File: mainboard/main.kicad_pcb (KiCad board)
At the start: 2 copper layers, 82.5 x 63.5 mm, 36 parts

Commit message: Updated component values in layout
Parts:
- Con_AddOn1: value Conn_01x05 -> Conn_01x09
- Con_P_Sw1: value Conn_01x04 -> Conn_01x02
- Con_RPi1: value Conn_01x05 -> Conn_01x08
- Con_Switch1: value Conn_01x04 -> Conn_01x03
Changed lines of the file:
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@@
       (effects (font (size 1 1) (thickness 0.15)))
     )
-    (fp_text value Conn_01x04 (at 2.54 -3.81 90) (layer F.Fab)
+    (fp_text value Conn_01x03 (at 2.54 -3.81 90) (layer F.Fab)
       (effects (font (size 1 1) (thickness 0.15)))
     )
@@
       (effects (font (size 1 1) (thickness 0.15)))
     )
-    (fp_text value Conn_01x05 (at 2.54 2.54 90) (layer F.Fab)
+    (fp_text value Conn_01x08 (at 2.54 2.54 90) (layer F.Fab)
       (effects (font (size 1 1) (thickness 0.15)))
     )
@@
       (effects (font (size 1 1) (thickness 0.15)))
     )
-    (fp_text value Conn_01x05 (at 17.145 2.54 90) (layer F.Fab)
+    (fp_text value Conn_01x09 (at 17.145 2.54 90) (layer F.Fab)
       (effects (font (size 1 1) (thickness 0.15)))
     )
@@
       (effects (font (size 1 1) (thickness 0.15)))
     )
-    (fp_text value Conn_01x04 (at 10.16 1.27) (layer F.Fab)
-      (effects (font (size 1 1) (thickness 0.15)))
-    )
+    (fp_text value Conn_01x02 (at 10.16 1.27) (layer F.Fab)
+      (effects (font (size 1 1) (thickness 0.15)))
+    )

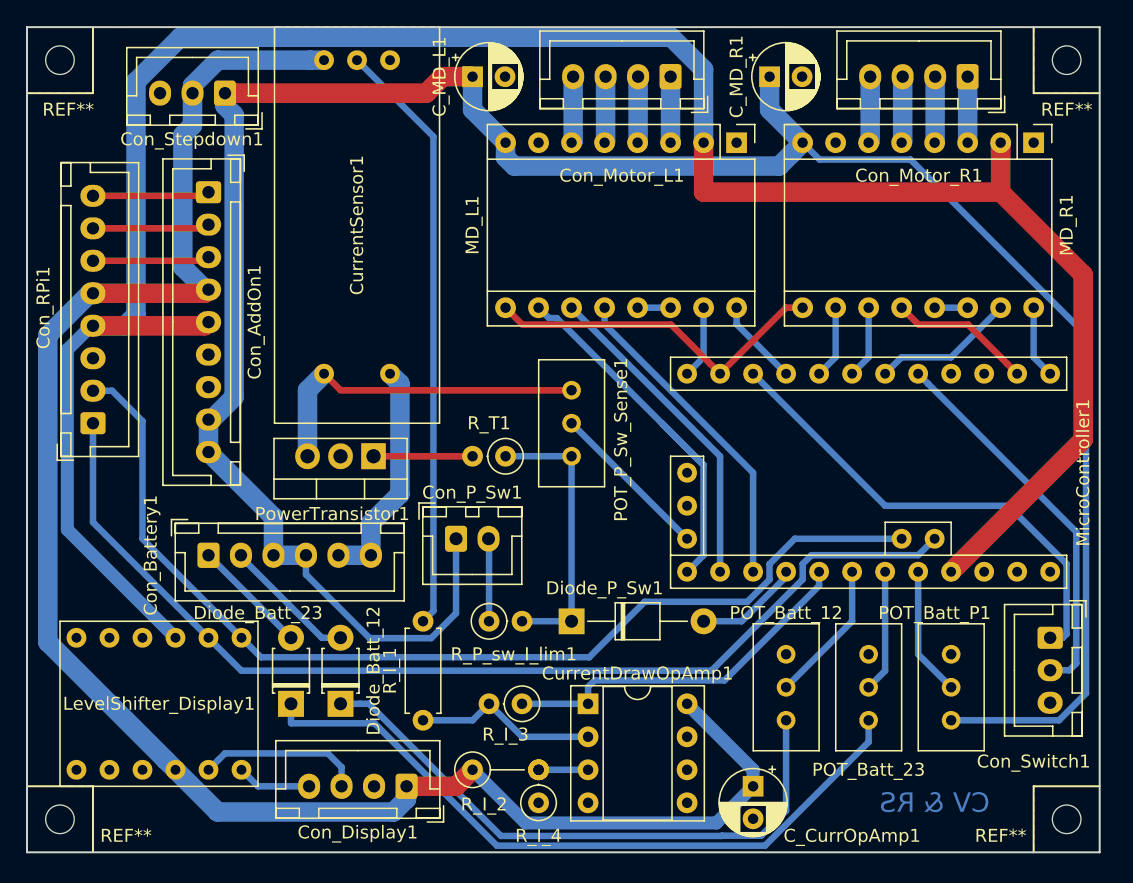
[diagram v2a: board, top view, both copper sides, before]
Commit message: New power circuitry and layout
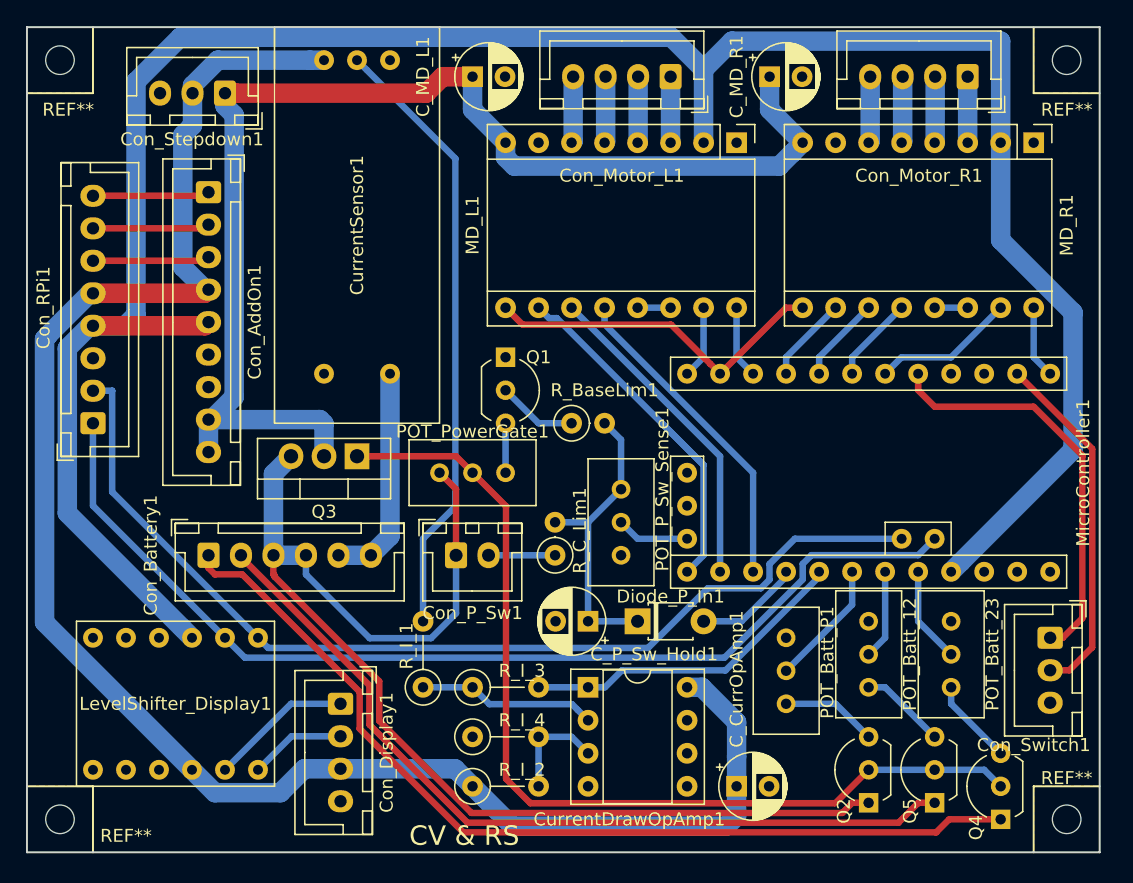
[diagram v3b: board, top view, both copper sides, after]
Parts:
- removed Diode_Batt_12, Diode_Batt_23: 1N 4448, Diode_THT:D_T-1_P5.08mm_Horizontal
- removed Diode_P_Sw1: 1N 4448, Diode_THT:D_T-1_P10.16mm_Horizontal
- removed PowerTransistor1: TIP120, Package_TO_SOT_THT:TO-220-3_Vertical
- removed R_P_sw_I_lim1: optional, Resistor_THT:R_Axial_DIN0207_L6.3mm_D2.5mm_P2.54mm_Vertical
- removed R_T1: 1K, Resistor_THT:R_Axial_DIN0207_L6.3mm_D2.5mm_P2.54mm_Vertical
- added C_P_Sw_Hold1: 100uF, Capacitor_THT:CP_Radial_D5.0mm_P2.50mm, F.Cu at (153.7, 72.4)
- added Diode_P_In1: 1N 4448, Diode_THT:D_T-1_P5.08mm_Horizontal, F.Cu at (157.5, 72.4)
- added POT_PowerGate1: 100K, Potentiometer_THT:Potentiometer_Bourns_3296W_Vertical, F.Cu at (142.2, 61.0)
- added Q1: 2N3904, Package_TO_SOT_THT:TO-92_Inline_Wide, F.Cu at (147.3, 52.1)
- added Q2: ZVP2106A, Package_TO_SOT_THT:TO-92L_Inline_Wide, F.Cu at (175.3, 86.4)
- added Q3: STP10P6F6, Package_TO_SOT_THT:TO-220-3_Vertical, F.Cu at (135.9, 59.7)
- added Q4: ZVP2106A, Package_TO_SOT_THT:TO-92L_Inline_Wide, F.Cu at (185.4, 87.6)
- added Q5: ZVP2106A, Package_TO_SOT_THT:TO-92L_Inline_Wide, F.Cu at (180.3, 86.4)
- added R_BaseLim1: 10k, Resistor_THT:R_Axial_DIN0207_L6.3mm_D2.5mm_P2.54mm_Vertical, F.Cu at (152.4, 57.1)
- added R_C_Lim1: 220, Resistor_THT:R_Axial_DIN0207_L6.3mm_D2.5mm_P2.54mm_Vertical, F.Cu at (151.1, 67.3)
- POT_Batt_12, POT_Batt_23, POT_Batt_P1: value 1M -> 100k
- POT_P_Sw_Sense1: value 50k -> 100K
- R_I_1: footprint Resistor_THT:R_Axial_DIN0207_L6.3mm_D2.5mm_P7.62mm_Horizontal -> Resistor_THT:R_Axial_DIN0207_L6.3mm_D2.5mm_P5.08mm_Vertical
- R_I_3, R_I_4: footprint Resistor_THT:R_Axial_DIN0207_L6.3mm_D2.5mm_P2.54mm_Vertical -> Resistor_THT:R_Axial_DIN0207_L6.3mm_D2.5mm_P5.08mm_Vertical
- moved POT_P_Sw_Sense1 13.3 mm to (156.2, 67.3), turned to 270 degrees
- moved POT_Batt_P1 12.8 mm to (168.9, 73.7)
- moved Con_Display1 8.13 mm to (134.6, 78.7), turned to 270 degrees
- moved R_I_4 7.18 mm to (144.8, 81.3), turned to 0 degrees
- moved POT_Batt_23 6.84 mm to (181.6, 72.4)
- moved POT_Batt_12 6.84 mm to (175.3, 72.4)
- moved R_I_1 5.08 mm to (141.0, 77.5), turned to 90 degrees
- moved R_I_3 4.02 mm to (144.8, 77.5), turned to 0 degrees
- moved C_CurrOpAmp1 1.27 mm to (165.1, 85.1), turned to 0 degrees
- moved LevelShifter_Display1 1.27 mm to (120.7, 78.7)
- moved R_I_2 1.27 mm to (144.8, 85.1)
- moved Con_P_Sw1 1.27 mm to (143.5, 67.3)
- moved CurrentDrawOpAmp1 1.27 mm to (153.7, 77.5)
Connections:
- C_MD_L1 pad 1: +BATT -> +12V
- C_MD_R1 pad 1: +BATT -> +12V
- Con_AddOn1 pad 8: +BATT -> +12V
- Con_AddOn1 pad 9: +BATT -> +12V
- Con_Display1 pad 1: +5V -> Net-(Con_Display1-Pad1)
- Con_Display1 pad 2: GND -> Net-(Con_Display1-Pad2)
- Con_Display1 pad 3: Net-(Con_Display1-Pad3) -> +5V
- Con_Display1 pad 4: Net-(Con_Display1-Pad4) -> GND
- Con_Stepdown1 pad 1: +BATT -> +12V
- CurrentSensor1 pad 5: Net-(CurrentSensor1-Pad5) -> GND
- LevelShifter_Display1 pad 11: Net-(Con_Display1-Pad3) -> Net-(Con_Display1-Pad1)
- LevelShifter_Display1 pad 12: Net-(Con_Display1-Pad4) -> Net-(Con_Display1-Pad2)
- MD_L1 pad 8: +BATT -> +12V
- MD_R1 pad 8: +BATT -> +12V
- MicroController1 pad 10: Sw2 -> Dir_L
- MicroController1 pad 2: MS3_R -> Sw1
- MicroController1 pad 20: ADC_Batt_12 -> ADC_Batt_P
- MicroController1 pad 21: ADC_Batt_23 -> ADC_Batt_12
- MicroController1 pad 23: ADC_Batt_P -> ADC_Batt_23
- MicroController1 pad 5: Sw1 -> Sw2
- MicroController1 pad 7: MS2_R -> MS3_R
- MicroController1 pad 8: MS1_R -> MS2_R
- MicroController1 pad 9: Dir_L -> MS1_R
- POT_Batt_P1 pad 3: +BATT -> Net-(POT_Batt_P1-Pad3)
- POT_P_Sw_Sense1 pad 1: Net-(CurrentSensor1-Pad5) -> GND
- R_I_1 pad 1: Net-(CurrentSensor1-Pad2) -> Net-(CurrentDrawOpAmp1-Pad2)
- R_I_1 pad 2: Net-(CurrentDrawOpAmp1-Pad2) -> Net-(CurrentSensor1-Pad2)
- R_I_3 pad 1: ADC_Batt_Curr -> Net-(CurrentDrawOpAmp1-Pad2)
- R_I_3 pad 2: Net-(CurrentDrawOpAmp1-Pad2) -> ADC_Batt_Curr
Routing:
- net +12V: track 0.00 -> 97.2 mm
- net +BATT: track 186.6 -> 94.9 mm
- net PowerGate: track 0.00 -> 74.5 mm
- net BATT_Cell_2_3: track 8.98 -> 72.4 mm
- net BATT_Cell_1_2: track 10.2 -> 64.4 mm
- net Net-(POT_Batt_23-Pad3): track 54.8 -> 6.66 mm
- net Net-(POT_Batt_12-Pad3): track 46.3 -> 6.66 mm
- net Net-(CurrentSensor1-Pad5): track 26.5 -> 0.00 mm
- net Net-(Con_Display1-Pad3): track 12.7 -> 0.00 mm
- net Net-(Con_Display1-Pad1): track 0.00 -> 11.0 mm
- net Net-(PowerTransistor1-Pad1): track 7.62 -> 0.00 mm
- net Net-(Con_Display1-Pad2): track 0.00 -> 7.42 mm
- net Net-(POT_Batt_P1-Pad3): track 0.00 -> 7.40 mm
- net P_Sw_Sense: track 12.6 -> 5.61 mm
- net Net-(Q1-Pad2): track 0.00 -> 6.13 mm
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
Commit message: - 200k potis for cell voltage sensing - hints on setting up the trim potis - Better layout of labels on PCB
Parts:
- POT_Batt_12, POT_Batt_23, POT_Batt_P1: value 100k -> 200k
